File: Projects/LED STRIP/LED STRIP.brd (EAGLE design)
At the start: 406.4 x 25.4 mm, 70 parts, among them U1 PCA9635, U2 PCA9635, U3 PCA9635

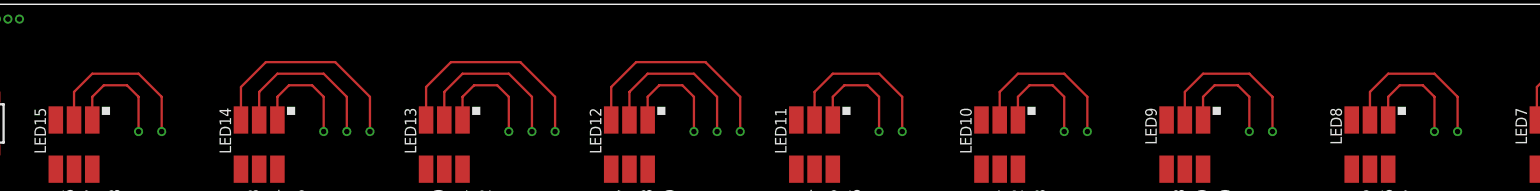
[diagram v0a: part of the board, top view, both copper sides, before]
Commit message: added traces that were accidentally deleted (from LED to via)
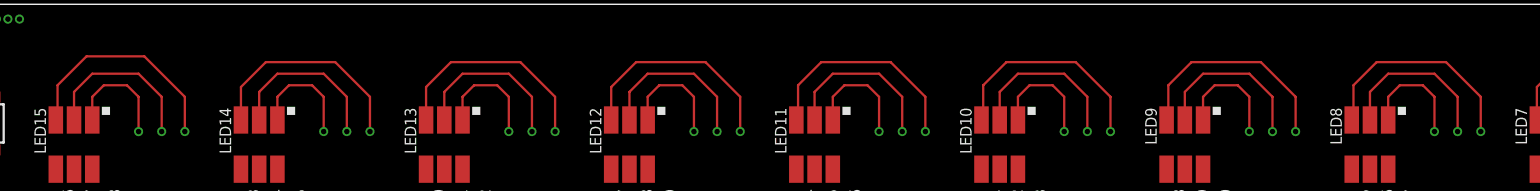
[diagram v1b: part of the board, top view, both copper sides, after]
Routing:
- net RED15: track 8.88 -> 33.8 mm, vias 1 -> 2
- net RED8: track 0.00 -> 24.3 mm, vias 1 -> 2
- net RED11: track 0.00 -> 24.3 mm, vias 1 -> 2
- net RED10: track 0.00 -> 24.3 mm, vias 1 -> 2
- net RED9: track 0.00 -> 24.3 mm, vias 1 -> 2
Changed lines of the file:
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@@
 <setting verticaltext="up"/>
 </settings>
-<grid distance="0.005" unitdist="mm" unit="mm" style="lines" multiple="1" display="no" altdistance="0.005" altunitdist="mm" altunit="mm"/>
+<grid distance="0.1" unitdist="inch" unit="inch" style="lines" multiple="1" display="no" altdistance="0.025" altunitdist="inch" altunit="inch"/>
 <layers>
 <layer number="1" name="Top" color="13" fill="1" visible="yes" active="yes"/>
@@
 <layer number="17" name="Pads" color="2" fill="1" visible="yes" active="yes"/>
 <layer number="18" name="Vias" color="2" fill="1" visible="yes" active="yes"/>
-<layer number="19" name="Unrouted" color="6" fill="1" visible="yes" active="yes"/>
+<layer number="19" name="Unrouted" color="6" fill="1" visible="no" active="yes"/>
 <layer number="20" name="Dimension" color="15" fill="1" visible="yes" active="yes"/>
 <layer number="21" name="tPlace" color="7" fill="1" visible="yes" active="yes"/>
@@
 <contactref element="LED15" pad="3"/>
 <via x="49.022" y="23.774" extent="1-16" drill="0.6"/>
-<wire x1="51.237" y1="15.219" x2="84.9" y2="12.7" width="0" layer="19" extent="1-1"/>
+<wire x1="99.06" y1="11.43" x2="51.237" y2="15.219" width="0" layer="19" extent="1-16"/>
 <wire x1="51.237" y1="15.219" x2="51.235" y2="16.375" width="0.254" layer="1"/>
 <wire x1="49.022" y1="23.774" x2="51.235" y2="16.375" width="0.254" layer="1"/>
+<wire x1="84.9" y1="12.7" x2="85.09" y2="12.7" width="0.254" layer="1"/>
+<wire x1="85.09" y1="12.7" x2="85.09" y2="16.51" width="0.254" layer="1"/>
+<wire x1="85.09" y1="16.51" x2="88.265" y2="19.685" width="0.254" layer="1"/>
+<wire x1="88.265" y1="19.685" x2="94.615" y2="19.685" width="0.254" layer="1"/>
+<wire x1="94.615" y1="19.685" x2="99.06" y2="15.24" width="0.254" layer="1"/>
+<wire x1="99.06" y1="15.24" x2="99.06" y2="11.43" width="0.254" layer="1"/>
+<via x="99.06" y="11.43" extent="1-16" drill="0.6"/>
 </signal>
 <signal name="RED14">
@@
 <contactref element="LED11" pad="3"/>
 <via x="54.102" y="23.774" extent="1-16" drill="0.6"/>
-<wire x1="53.837" y1="15.219" x2="166.18" y2="12.7" width="0" layer="19" extent="1-1"/>
+<wire x1="180.34" y1="11.43" x2="53.837" y2="15.219" width="0" layer="19" extent="1-16"/>
 <wire x1="54.102" y1="23.774" x2="53.837" y2="15.219" width="0" layer="19" extent="1-1"/>
+<wire x1="166.18" y1="12.7" x2="166.37" y2="12.89" width="0.254" layer="1"/>
+<wire x1="166.37" y1="12.89" x2="166.37" y2="16.51" width="0.254" layer="1"/>
+<wire x1="166.37" y1="16.51" x2="168.91" y2="19.05" width="0.254" layer="1"/>
+<wire x1="168.91" y1="19.05" x2="176.53" y2="19.05" width="0.254" layer="1"/>
+<wire x1="176.53" y1="19.05" x2="180.34" y2="15.24" width="0.254" layer="1"/>
+<wire x1="180.34" y1="15.24" x2="180.34" y2="11.43" width="0.254" layer="1"/>
+<via x="180.34" y="11.43" extent="1-16" drill="0.6"/>
 </signal>
 <signal name="RED10">
@@
 <contactref element="LED10" pad="3"/>
 <via x="55.372" y="23.774" extent="1-16" drill="0.6"/>
-<wire x1="55.372" y1="23.774" x2="186.5" y2="12.7" width="0" layer="19" extent="1-1"/>
+<wire x1="200.66" y1="11.43" x2="55.372" y2="23.774" width="0" layer="19" extent="1-16"/>
 <wire x1="54.487" y1="15.219" x2="55.372" y2="23.774" width="0" layer="19" extent="1-1"/>
+<wire x1="186.5" y1="12.7" x2="186.69" y2="12.89" width="0.254" layer="1"/>
+<wire x1="186.69" y1="12.89" x2="186.69" y2="16.51" width="0.254" layer="1"/>
+<wire x1="186.69" y1="16.51" x2="189.23" y2="19.05" width="0.254" layer="1"/>
+<wire x1="189.23" y1="19.05" x2="196.85" y2="19.05" width="0.254" layer="1"/>
+<wire x1="196.85" y1="19.05" x2="200.66" y2="15.24" width="0.254" layer="1"/>
+<wire x1="200.66" y1="15.24" x2="200.66" y2="11.43" width="0.254" layer="1"/>
+<via x="200.66" y="11.43" extent="1-16" drill="0.6"/>
 </signal>
 <signal name="RED9">
@@
 <contactref element="LED9" pad="3"/>
 <via x="56.642" y="23.774" extent="1-16" drill="0.6"/>
-<wire x1="56.642" y1="23.774" x2="206.82" y2="12.7" width="0" layer="19" extent="1-1"/>
+<wire x1="220.98" y1="11.43" x2="56.642" y2="23.774" width="0" layer="19" extent="1-16"/>
 <wire x1="55.137" y1="15.219" x2="56.642" y2="23.774" width="0" layer="19" extent="1-1"/>
+<wire x1="206.82" y1="12.7" x2="207.01" y2="12.89" width="0.254" layer="1"/>
+<wire x1="207.01" y1="12.89" x2="207.01" y2="16.51" width="0.254" layer="1"/>
+<wire x1="207.01" y1="16.51" x2="209.55" y2="19.05" width="0.254" layer="1"/>
+<wire x1="209.55" y1="19.05" x2="217.17" y2="19.05" width="0.254" layer="1"/>
+<wire x1="217.17" y1="19.05" x2="220.98" y2="15.24" width="0.254" layer="1"/>
+<wire x1="220.98" y1="15.24" x2="220.98" y2="11.43" width="0.254" layer="1"/>
+<via x="220.98" y="11.43" extent="1-16" drill="0.6"/>
 </signal>
 <signal name="RED8">
@@
 <contactref element="LED8" pad="3"/>
 <via x="57.912" y="23.774" extent="1-16" drill="0.6"/>
-<wire x1="57.912" y1="23.774" x2="227.14" y2="12.7" width="0" layer="19" extent="1-1"/>
+<wire x1="241.3" y1="11.43" x2="57.912" y2="23.774" width="0" layer="19" extent="1-16"/>
 <wire x1="55.787" y1="15.219" x2="57.912" y2="23.774" width="0" layer="19" extent="1-1"/>
+<wire x1="227.14" y1="12.7" x2="227.33" y2="12.89" width="0.254" layer="1"/>
+<wire x1="227.33" y1="12.89" x2="227.33" y2="16.51" width="0.254" layer="1"/>
+<wire x1="227.33" y1="16.51" x2="229.87" y2="19.05" width="0.254" layer="1"/>
+<wire x1="229.87" y1="19.05" x2="237.49" y2="19.05" width="0.254" layer="1"/>
+<wire x1="237.49" y1="19.05" x2="241.3" y2="15.24" width="0.254" layer="1"/>
+<wire x1="241.3" y1="15.24" x2="241.3" y2="11.43" width="0.254" layer="1"/>
+<via x="241.3" y="11.43" extent="1-16" drill="0.6"/>
 </signal>
 <signal name="GREEN0">
